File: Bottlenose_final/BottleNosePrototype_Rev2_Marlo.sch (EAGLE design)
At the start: 31 parts, among them Q1 8/16/20MHz, U1 MCP73831, U2 FT232RLSSOP, X1 USB-SMD-NS

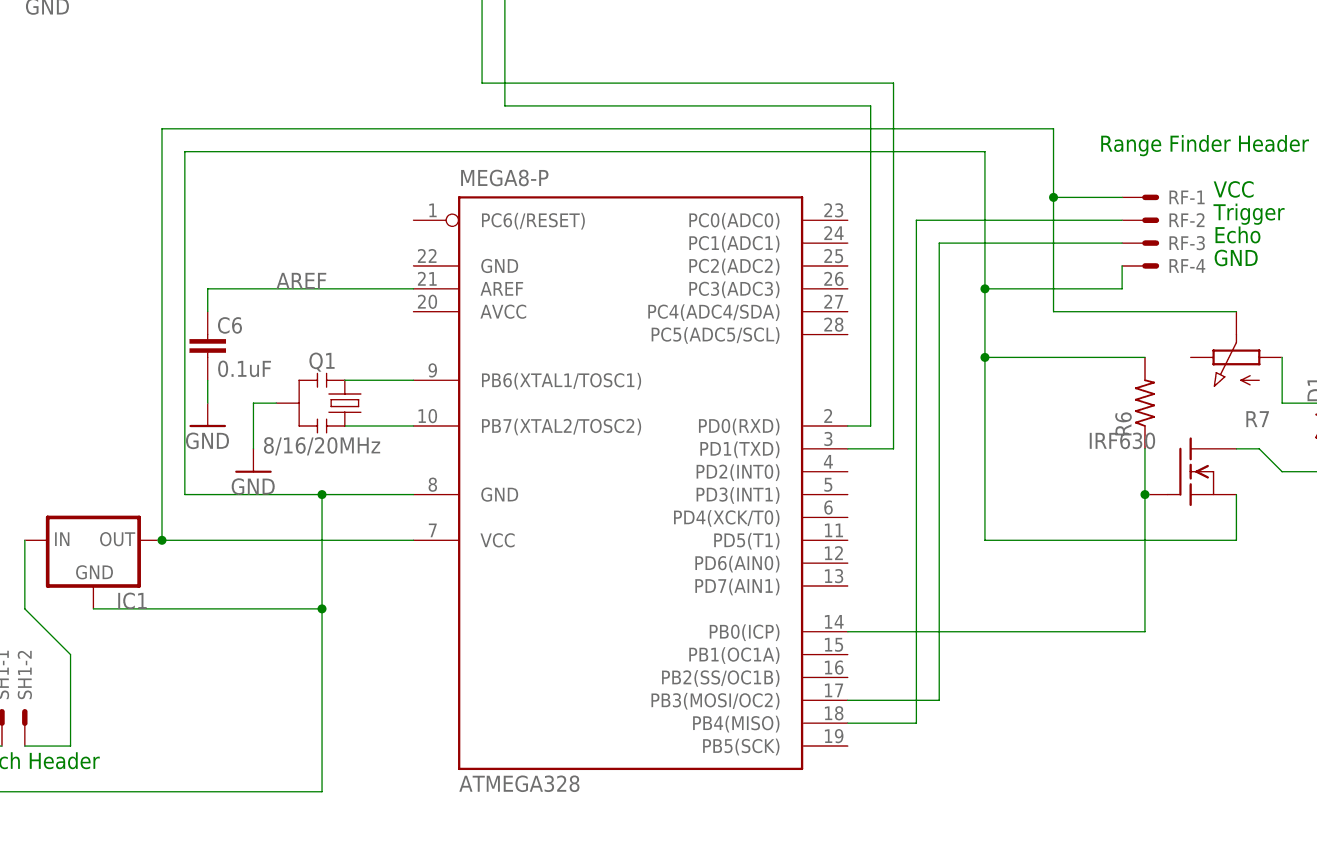
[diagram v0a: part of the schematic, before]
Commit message: Modified the .sch to meet current and only working build of bottlenose.
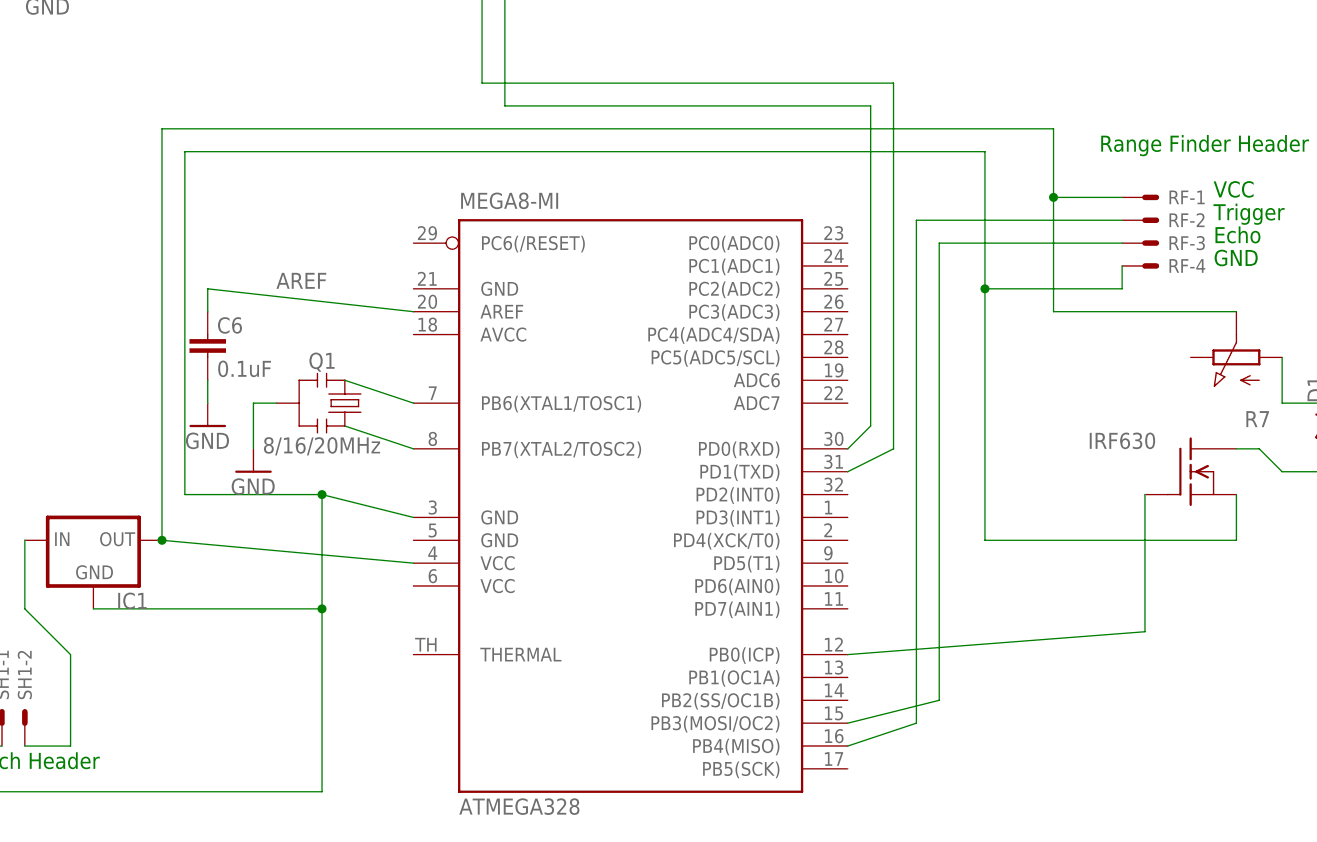
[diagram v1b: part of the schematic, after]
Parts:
- removed R6: (no value), rcl:R-US_0204/5
- ATMEGA328: value MEGA8-P -> MEGA8-MI; device atmel:MEGA8-P -> atmel:MEGA8-MI; MPN (none) -> ATMEGA88PA-MU; OC_FARNELL (none) -> 1715491; OC_NEWARK (none) -> 15R0272
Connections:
- net N$1: no longer R6.1
- net N$6: no longer R6.2
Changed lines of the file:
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@@
 </classes>
 <parts>
-<part name="ATMEGA328" library="atmel" deviceset="MEGA8-P" device=""/>
+<part name="ATMEGA328" library="atmel" deviceset="MEGA8-MI" device="">
+<attribute name="MPN" value="ATMEGA88PA-MU"/>
+<attribute name="OC_FARNELL" value="1715491"/>
+<attribute name="OC_NEWARK" value="15R0272"/>
+</part>
 <part name="RF" library="con-molex" deviceset="22-23-2041" device="" value=""/>
 <part name="IRF630" library="transistor-fet" deviceset="IRF620" device="" value=""/>
@@
 <part name="IC1" library="v-reg" deviceset="78LXX" device=""/>
 <part name="D1" library="diode" deviceset="1N4004" device=""/>
-<part name="R6" library="rcl" deviceset="R-US_" device="0204/5"/>
 <part name="R8" library="rcl" deviceset="R-US_" device="0204/5"/>
 <part name="SH1" library="con-molex" deviceset="22-23-2021" device="" value=""/>
@@
 <instance part="IC1" gate="1" x="17.78" y="35.56"/>
 <instance part="D1" gate="1" x="154.94" y="48.26" rot="R90"/>
-<instance part="R6" gate="G$1" x="134.62" y="50.8" rot="R90"/>
 <instance part="R8" gate="G$1" x="165.1" y="50.8"/>
 <instance part="SH1" gate="-1" x="7.62" y="15.24" rot="R90"/>
@@
 <segment>
 <pinref part="ATMEGA328" gate="G$1" pin="PB3(MOSI/OC2)"/>
-<wire x1="101.6" y1="17.78" x2="111.76" y2="17.78" width="0.1524" layer="91"/>
+<wire x1="101.6" y1="15.24" x2="111.76" y2="17.78" width="0.1524" layer="91"/>
 <wire x1="111.76" y1="17.78" x2="111.76" y2="68.58" width="0.1524" layer="91"/>
 <pinref part="RF" gate="-3" pin="S"/>
@@
 <segment>
 <pinref part="ATMEGA328" gate="G$1" pin="PB4(MISO)"/>
-<wire x1="101.6" y1="15.24" x2="109.22" y2="15.24" width="0.1524" layer="91"/>
+<wire x1="101.6" y1="12.7" x2="109.22" y2="15.24" width="0.1524" layer="91"/>
 <wire x1="109.22" y1="15.24" x2="109.22" y2="71.12" width="0.1524" layer="91"/>
 <pinref part="RF" gate="-2" pin="S"/>
@@
 <pinref part="U2" gate="G$1" pin="TXD"/>
 <pinref part="ATMEGA328" gate="G$1" pin="PD0(RXD)"/>
-<wire x1="101.6" y1="48.26" x2="104.14" y2="48.26" width="0.1524" layer="91"/>
+<wire x1="101.6" y1="45.72" x2="104.14" y2="48.26" width="0.1524" layer="91"/>
 <wire x1="104.14" y1="48.26" x2="104.14" y2="83.82" width="0.1524" layer="91"/>
 <wire x1="104.14" y1="83.82" x2="63.5" y2="83.82" width="0.1524" layer="91"/>
@@
 <pinref part="U2" gate="G$1" pin="RXD"/>
 <pinref part="ATMEGA328" gate="G$1" pin="PD1(TXD)"/>
-<wire x1="101.6" y1="45.72" x2="106.68" y2="45.72" width="0.1524" layer="91"/>
+<wire x1="101.6" y1="43.18" x2="106.68" y2="45.72" width="0.1524" layer="91"/>
 <wire x1="106.68" y1="45.72" x2="106.68" y2="86.36" width="0.1524" layer="91"/>
 <wire x1="106.68" y1="86.36" x2="60.96" y2="86.36" width="0.1524" layer="91"/>
@@
 <net name="AREF" class="0">
 <segment>
-<wire x1="53.34" y1="63.5" x2="30.48" y2="63.5" width="0.1524" layer="91"/>
+<wire x1="53.34" y1="60.96" x2="30.48" y2="63.5" width="0.1524" layer="91"/>
 <wire x1="30.48" y1="63.5" x2="30.48" y2="60.96" width="0.1524" layer="91"/>
 <label x="38.1" y="63.5" size="1.778" layer="95"/>
@@
 <pinref part="Q1" gate="G$1" pin="1"/>
 <pinref part="ATMEGA328" gate="G$1" pin="PB7(XTAL2/TOSC2)"/>
-<wire x1="53.34" y1="48.26" x2="45.72" y2="48.26" width="0.1524" layer="91"/>
+<wire x1="53.34" y1="45.72" x2="45.72" y2="48.26" width="0.1524" layer="91"/>
 </segment>
 </net>
@@
 <pinref part="Q1" gate="G$1" pin="3"/>
 <pinref part="ATMEGA328" gate="G$1" pin="PB6(XTAL1/TOSC1)"/>
-<wire x1="53.34" y1="53.34" x2="45.72" y2="53.34" width="0.1524" layer="91"/>
+<wire x1="53.34" y1="50.8" x2="45.72" y2="53.34" width="0.1524" layer="91"/>
 </segment>
 </net>
@@
 <segment>
 <pinref part="ATMEGA328" gate="G$1" pin="VCC@1"/>
-<wire x1="53.34" y1="35.56" x2="25.4" y2="35.56" width="0.1524" layer="91"/>
+<wire x1="53.34" y1="33.02" x2="25.4" y2="35.56" width="0.1524" layer="91"/>
 <wire x1="25.4" y1="35.56" x2="25.4" y2="81.28" width="0.1524" layer="91"/>
 <wire x1="25.4" y1="81.28" x2="124.46" y2="81.28" width="0.1524" layer="91"/>
@@
 <pinref part="IRF630" gate="G$1" pin="G"/>
 <wire x1="134.62" y1="25.4" x2="134.62" y2="40.64" width="0.1524" layer="91"/>
-<pinref part="R6" gate="G$1" pin="1"/>
-<wire x1="134.62" y1="40.64" x2="134.62" y2="45.72" width="0.1524" layer="91"/>
 <pinref part="ATMEGA328" gate="G$1" pin="PB0(ICP)"/>
-<wire x1="101.6" y1="25.4" x2="134.62" y2="25.4" width="0.1524" layer="91"/>
-<junction x="134.62" y="40.64"/>
+<wire x1="101.6" y1="22.86" x2="134.62" y2="25.4" width="0.1524" layer="91"/>
 </segment>
 </net>
@@
 <wire x1="0" y1="7.62" x2="43.18" y2="7.62" width="0.1524" layer="91"/>
 <pinref part="ATMEGA328" gate="G$1" pin="GND@1"/>
-<wire x1="53.34" y1="40.64" x2="43.18" y2="40.64" width="0.1524" layer="91"/>
+<wire x1="53.34" y1="38.1" x2="43.18" y2="40.64" width="0.1524" layer="91"/>
 <wire x1="43.18" y1="40.64" x2="27.94" y2="40.64" width="0.1524" layer="91"/>
 <wire x1="27.94" y1="40.64" x2="27.94" y2="78.74" width="0.1524" layer="91"/>
@@
 <wire x1="116.84" y1="63.5" x2="132.08" y2="63.5" width="0.1524" layer="91"/>
 <wire x1="132.08" y1="63.5" x2="132.08" y2="66.04" width="0.1524" layer="91"/>
-<wire x1="116.84" y1="35.56" x2="116.84" y2="55.88" width="0.1524" layer="91"/>
+<wire x1="116.84" y1="35.56" x2="116.84" y2="63.5" width="0.1524" layer="91"/>
 <junction x="116.84" y="63.5"/>
-<wire x1="116.84" y1="55.88" x2="116.84" y2="63.5" width="0.1524" layer="91"/>
-<junction x="116.84" y="55.88"/>
-<wire x1="134.62" y1="55.88" x2="116.84" y2="55.88" width="0.1524" layer="91"/>
 <wire x1="43.18" y1="40.64" x2="43.18" y2="27.94" width="0.1524" layer="91"/>
 <wire x1="43.18" y1="27.94" x2="43.18" y2="7.62" width="0.1524" layer="91"/>
@@
 <wire x1="17.78" y1="27.94" x2="43.18" y2="27.94" width="0.1524" layer="91"/>
 <junction x="43.18" y="27.94"/>
-<pinref part="R6" gate="G$1" pin="2"/>
 <pinref part="IRF630" gate="G$1" pin="S"/>
 <wire x1="144.78" y1="40.64" x2="144.78" y2="35.56" width="0.1524" layer="91"/>
